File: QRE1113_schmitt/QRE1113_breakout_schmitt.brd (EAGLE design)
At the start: 11.2 x 19.1 mm, 8 parts, among them IC1 74AUC1G17DBV, IC2 QRE1113, Q1 2N3904

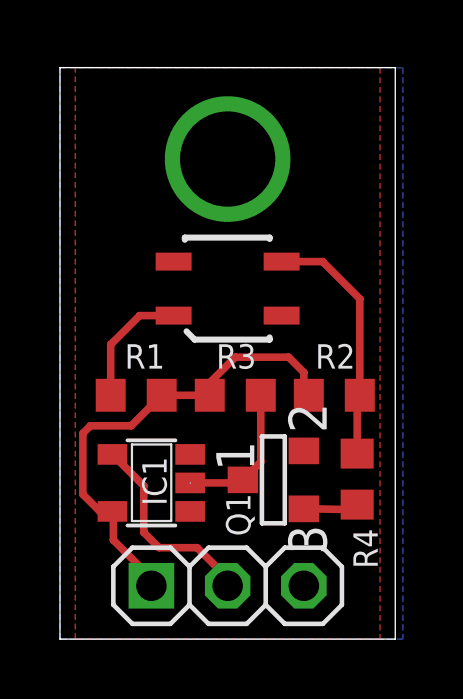
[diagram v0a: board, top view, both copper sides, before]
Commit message: Initial version of qre1113 breakout with onboard schmitt
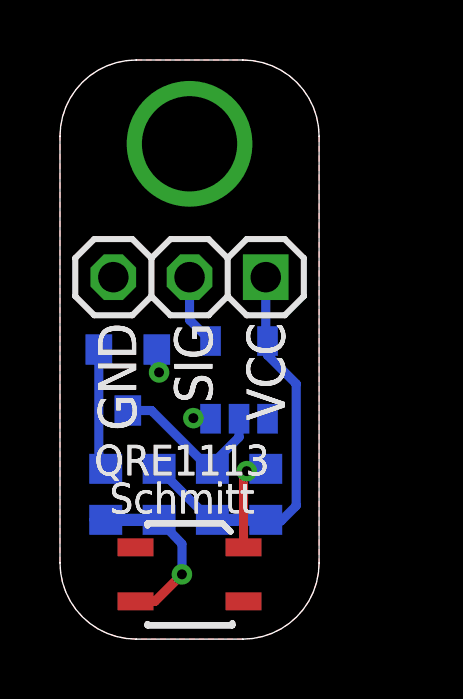
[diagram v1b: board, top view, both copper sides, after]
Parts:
- R2, R3: value 2.2k -> 2k2
- moved JP1 10.4 mm to (4.32, 12.1), turned to 180 degrees
- moved IC2 9.61 mm to (4.32, 2.16), turned to 180 degrees
- moved R4 8.40 mm to (1.52, 4.83), flipped to the bottom, turned to 90 degrees
- moved R2 6.71 mm to (3.30, 4.83), flipped to the bottom, turned to 90 degrees
- moved Q1 5.85 mm to (2.29, 8.64), flipped to the bottom, turned to 0 degrees
- moved R1 5.44 mm to (6.86, 4.83), flipped to the bottom, turned to 270 degrees
- moved IC1 4.50 mm to (5.97, 8.64), flipped to the bottom, turned to 0 degrees
- moved R3 3.39 mm to (5.08, 4.83), flipped to the bottom, turned to 270 degrees
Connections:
- net N$3 renamed SIG
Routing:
- net SIG: track 6.71 -> 2.42 mm
- net VCC: track 16.0 -> 13.5 mm
- net N$5: track 1.87 -> 4.07 mm
- net N$1: track 8.31 -> 6.38 mm, vias 0 -> 1
- net GND: track 0.00 -> 1.37 mm, vias 1 -> 3
- net N$2: track 4.19 -> 3.25 mm, vias 0 -> 1
- net N$4: track 4.87 -> 5.66 mm
- removed copper zone on layer 16, net GND
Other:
- board size 11.2 x 19.1 mm -> 8.6 x 19.3 mm
- board text added: "100"
- board text added: "2k2"
- board text removed: "Breakout"
- board text removed: "bot-thoughts.com"
